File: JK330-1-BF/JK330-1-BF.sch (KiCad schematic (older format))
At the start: 16 parts, among them K1 CONN_2, K10 COLONETTE, K2 CONN_2, K3 CONN_3, K4 CONN_2, K5 COLONETTE, K6 COLONETTE, K7 COLONETTE, K8 COLONETTE, K9 COLONETTE, P1 U.FL, P2 U.FL, P3 U.FL, P4 CONN_5, P5 HE10-16, P6 CONN_6

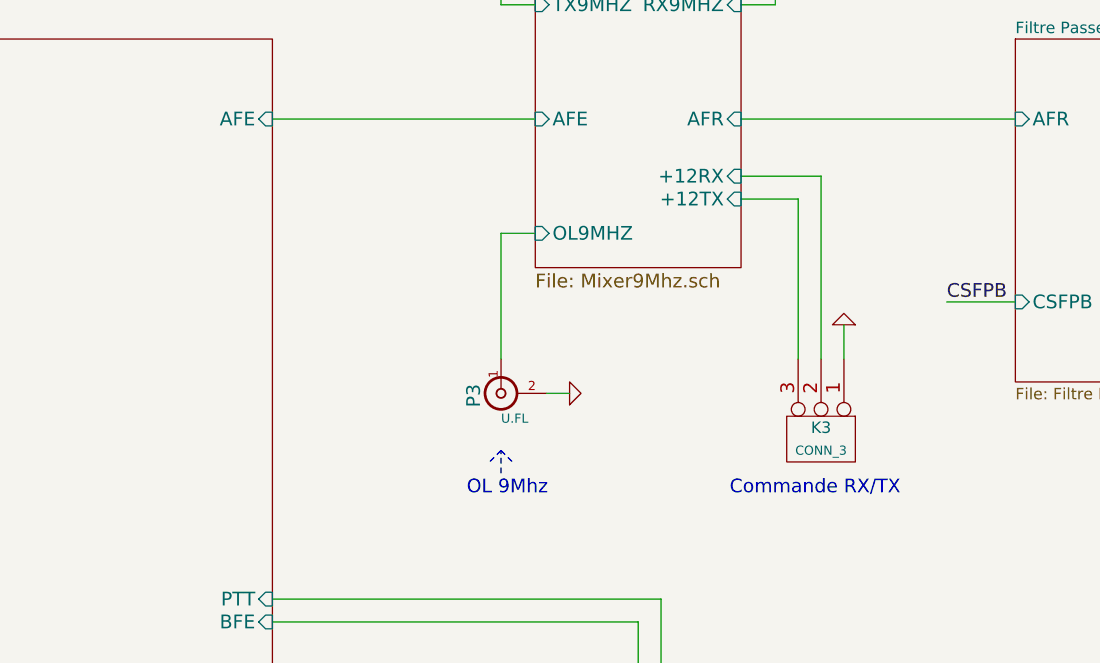
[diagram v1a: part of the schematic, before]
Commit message: Rajout commande PTT
+12VTV
+12VRX
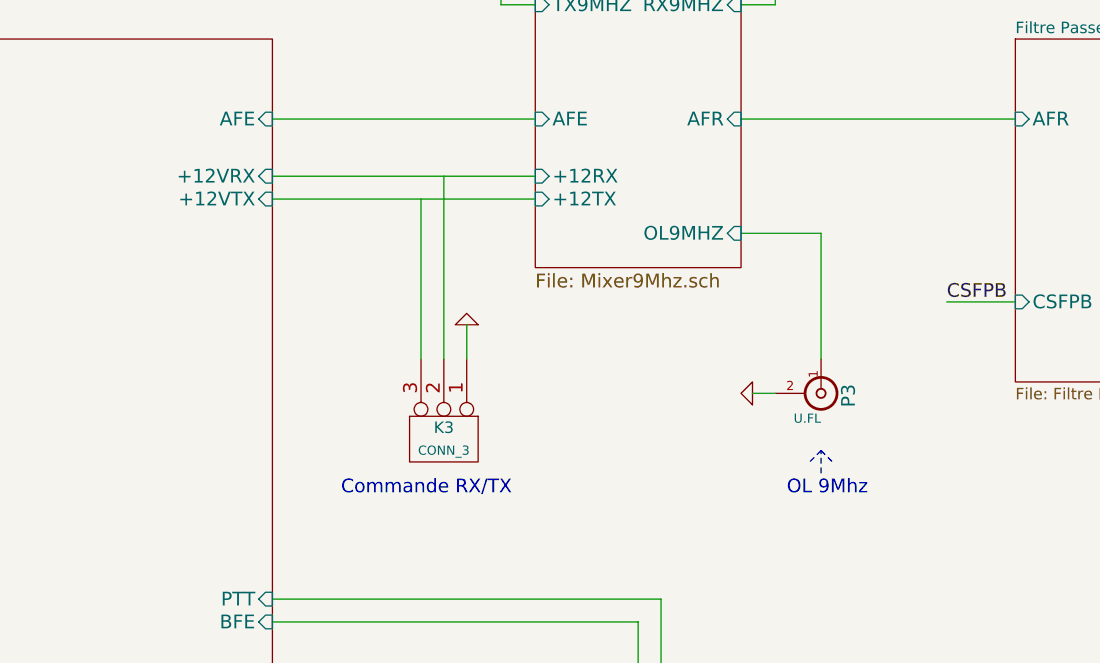
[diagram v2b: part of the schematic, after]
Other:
- moved on the sheet: K3, P3
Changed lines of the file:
@@
-EESchema Schematic File Version 2  date 29/04/2013 22:12:34
+EESchema Schematic File Version 2  date 30/04/2013 22:23:42
 LIBS:power
 LIBS:CEN-SCHEMA
@@
 Sheet 1 6
 Title ""
-Date "29 apr 2013"
+Date "30 apr 2013"
 Rev ""
 Comp ""
@@
 L GND #PWR01
 U 1 1 514E3278
-P 3950 3850
-F 0 "#PWR01" H 3950 3850 30  0001 C CNN
-F 1 "GND" H 3950 3780 30  0001 C CNN
-F 2 "" H 3950 3850 60  0001 C CNN
-F 3 "" H 3950 3850 60  0001 C CNN
-	1    3950 3850
-	0    -1   -1   0
+P 4750 3850
+F 0 "#PWR01" H 4750 3850 30  0001 C CNN
+F 1 "GND" H 4750 3780 30  0001 C CNN
+F 2 "" H 4750 3850 60  0001 C CNN
+F 3 "" H 4750 3850 60  0001 C CNN
+	1    4750 3850
+	0    1    -1   0
 $EndComp
 $Comp
@@
 $EndComp
 Wire Wire Line
-	3850 3850 3950 3850
-Wire Wire Line
-	4950 3700 4950 3000
-Wire Wire Line
-	4950 3000 4700 3000
-Wire Wire Line
-	3650 3700 3650 3150
-Wire Wire Line
-	3650 3150 3800 3150
+	4850 3850 4750 3850
+Wire Wire Line
+	3300 3700 3300 3000
+Wire Wire Line
+	5050 3700 5050 3150
 Wire Wire Line
 	3800 2650 2650 2650
@@
 	4700 2650 5900 2650
 Wire Wire Line
-	4700 2900 5050 2900
-Wire Wire Line
-	5050 2900 5050 3700
+	3400 2900 3400 3700
 Wire Wire Line
 	5850 6400 5850 6250
@@
 F0 "Mixer 9Mhz" 60
 F1 "Mixer9Mhz.sch" 60
-F2 "OL9MHZ" I L 3800 3150 60
-F3 "+12RX" I R 4700 2900 60
-F4 "+12TX" I R 4700 3000 60
+F2 "OL9MHZ" I R 4700 3150 60
+F3 "+12RX" I L 3800 2900 60
+F4 "+12TX" I L 3800 3000 60
 F5 "RX9MHZ" I R 4700 2150 60
 F6 "TX9MHZ" I L 3800 2150 60
@@
 F3 "BFE" I R 2650 4850 60
 F4 "AFE" I R 2650 2650 60
+F5 "+12VRX" I R 2650 2900 60
+F6 "+12VTX" I R 2650 3000 60
 $EndSheet
 Wire Notes Line
-	3650 4200 3650 4100
-Wire Notes Line
-	3650 4100 3600 4150
-Wire Notes Line
-	3650 4100 3700 4150
-Text Notes 3500 4300 0    60   ~ 0
+	5050 4200 5050 4100
+Wire Notes Line
+	5050 4100 5000 4150
+Wire Notes Line
+	5050 4100 5100 4150
+Text Notes 4900 4300 0    60   ~ 0
 OL 9Mhz
-Text Notes 4650 4300 0    60   ~ 0
+Text Notes 2950 4300 0    60   ~ 0
 Commande RX/TX\n
 $Comp
@@
 L CONN_3 K3
 U 1 1 514F8C00
-P 5050 4050
-F 0 "K3" V 5000 4050 50  0000 C CNN
-F 1 "CONN_3" V 5100 4050 40  0000 C CNN
-F 2 "" H 5050 4050 60  0000 C CNN
-F 3 "" H 5050 4050 60  0000 C CNN
-	1    5050 4050
-	0    1    1    0
-$EndComp
-Wire Wire Line
-	5150 3700 5150 3550
+P 3400 4050
+F 0 "K3" V 3350 4050 50  0000 C CNN
+F 1 "CONN_3" V 3450 4050 40  0000 C CNN
+F 2 "" H 3400 4050 60  0000 C CNN
+F 3 "" H 3400 4050 60  0000 C CNN
+	1    3400 4050
+	0    1    1    0
+$EndComp
+Wire Wire Line
+	3500 3700 3500 3550
 $Comp
 L GND #PWR014
 U 1 1 514F8DE0
-P 5150 3550
-F 0 "#PWR014" H 5150 3550 30  0001 C CNN
-F 1 "GND" H 5150 3480 30  0001 C CNN
-F 2 "" H 5150 3550 60  0000 C CNN
-F 3 "" H 5150 3550 60  0000 C CNN
-	1    5150 3550
+P 3500 3550
+F 0 "#PWR014" H 3500 3550 30  0001 C CNN
+F 1 "GND" H 3500 3480 30  0001 C CNN
+F 2 "" H 3500 3550 60  0000 C CNN
+F 3 "" H 3500 3550 60  0000 C CNN
+	1    3500 3550
 	-1   0    0    1
 $EndComp
@@
 L U.FL P3
 U 1 1 514F7AA8
-P 3650 3850
-F 0 "P3" H 3660 3970 60  0000 C CNN
-F 1 "U.FL" V 3760 3790 40  0000 C CNN
-F 2 "~" H 3650 3850 60  0000 C CNN
-F 3 "~" H 3650 3850 60  0000 C CNN
-	1    3650 3850
-	0    -1   1    0
+P 5050 3850
+F 0 "P3" H 5060 3970 60  0000 C CNN
+F 1 "U.FL" V 5160 3790 40  0000 C CNN
+F 2 "~" H 5050 3850 60  0000 C CNN
+F 3 "~" H 5050 3850 60  0000 C CNN
+	1    5050 3850
+	0    1    1    0
 $EndComp
 $Comp
@@
 	1    0    0    -1
 $EndComp
+Wire Wire Line
+	2650 2900 3800 2900
+Wire Wire Line
+	2650 3000 3800 3000
+Wire Wire Line
+	5050 3150 4700 3150
 $EndSCHEMATC

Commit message: Routage  PCB
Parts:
- added K11: CONN_3, symbol CONN_3
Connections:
- wire segments 54 -> 58
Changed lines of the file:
@@
-EESchema Schematic File Version 2  date 04/06/2013 21:43:31
+EESchema Schematic File Version 2  date 09/06/2013 23:13:58
 LIBS:power
 LIBS:CEN-SCHEMA
@@
 Sheet 1 6
 Title ""
-Date "4 jun 2013"
+Date "9 jun 2013"
 Rev ""
 Comp ""
@@
 F1 "Mixer9Mhz.sch" 60
 F2 "OL9MHZ" I R 4700 3150 60
-F3 "+12RX" I L 3800 2900 60
-F4 "+12TX" I L 3800 3000 60
-F5 "RX9MHZ" I R 4700 2150 60
-F6 "TX9MHZ" I L 3800 2150 60
-F7 "AFE" I L 3800 2650 60
-F8 "AFR" I R 4700 2650 60
+F3 "RX9MHZ" I R 4700 2150 60
+F4 "TX9MHZ" I L 3800 2150 60
+F5 "AFE" I L 3800 2650 60
+F6 "AFR" I R 4700 2650 60
+F7 "+12VRX" I L 3800 2900 60
+F8 "+12VTX" I L 3800 3000 60
 $EndSheet
 $Sheet
@@
 F1 "HP.sch" 50
 F2 "LINEOUT" I R 9650 2650 60
-F3 "AFRN" I L 8850 2650 60
-F4 "HP1" I R 9650 3300 60
-F5 "HP2" I R 9650 3550 60
+F3 "HP1" I R 9650 3300 60
+F4 "HP2" I R 9650 3550 60
+F5 "BFIN" I L 8850 2650 60
 $EndSheet
 Wire Wire Line
 	6750 2650 7450 2650
-Wire Wire Line
-	8300 2650 8850 2650
 Wire Wire Line
 	9650 3550 10100 3550
@@
 F 3 "" H 8150 6500 60  0000 C CNN
 	1    8150 6500
-	-1   0    0    1
+	1    0    0    1
 $EndComp
 Entry Wire Line
@@
 Wire Wire Line
 	5050 3150 4700 3150
+Connection ~ 3400 2900
+Connection ~ 3300 3000
+$Comp
+L CONN_3 K11
+U 1 1 51B4E722
+P 8600 1800
+F 0 "K11" V 8550 1800 50  0000 C CNN
+F 1 "CONN_3" V 8650 1800 40  0000 C CNN
+F 2 "" H 8600 1800 60  0000 C CNN
+F 3 "" H 8600 1800 60  0000 C CNN
+	1    8600 1800
+	0    -1   -1   0
+$EndComp
+Wire Wire Line
+	8300 2650 8600 2650
+Wire Wire Line
+	8600 2650 8600 2150
+Wire Wire Line
+	8850 2650 8700 2650
+Wire Wire Line
+	8700 2650 8700 2150
+Wire Wire Line
+	8500 2150 8500 2250
+$Comp
+L GND #PWR017
+U 1 1 51B4E972
+P 8500 2250
+F 0 "#PWR017" H 8500 2250 30  0001 C CNN
+F 1 "GND" H 8500 2180 30  0001 C CNN
+F 2 "" H 8500 2250 60  0000 C CNN
+F 3 "" H 8500 2250 60  0000 C CNN
+	1    8500 2250
+	1    0    0    -1
+$EndComp
 $EndSCHEMATC

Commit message: Reste 2 pistes a router
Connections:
- net labels removed: +BATT
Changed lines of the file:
@@
-EESchema Schematic File Version 2  date 09/06/2013 23:13:58
+EESchema Schematic File Version 2  date 11/06/2013 22:16:43
 LIBS:power
 LIBS:CEN-SCHEMA
@@
 Sheet 1 6
 Title ""
-Date "9 jun 2013"
+Date "11 jun 2013"
 Rev ""
 Comp ""
@@
 $EndComp
 $Comp
-L +BATT #PWR016
-U 1 1 514F93C1
-P 2500 6650
-F 0 "#PWR016" H 2500 6600 20  0001 C CNN
-F 1 "+BATT" H 2500 6750 30  0000 C CNN
-F 2 "" H 2500 6650 60  0000 C CNN
-F 3 "" H 2500 6650 60  0000 C CNN
-	1    2500 6650
-	1    0    0    -1
-$EndComp
-$Comp
 L U.FL P1
 U 1 1 514F77BA
@@
 F 3 "" H 8600 1800 60  0000 C CNN
 	1    8600 1800
-	0    -1   -1   0
-$EndComp
-Wire Wire Line
-	8300 2650 8600 2650
-Wire Wire Line
-	8600 2650 8600 2150
-Wire Wire Line
-	8850 2650 8700 2650
-Wire Wire Line
-	8700 2650 8700 2150
-Wire Wire Line
-	8500 2150 8500 2250
-$Comp
-L GND #PWR017
+	0    1    -1   0
+$EndComp
+Wire Wire Line
+	8700 2150 8700 2250
+$Comp
+L GND #PWR016
 U 1 1 51B4E972
-P 8500 2250
-F 0 "#PWR017" H 8500 2250 30  0001 C CNN
-F 1 "GND" H 8500 2180 30  0001 C CNN
-F 2 "" H 8500 2250 60  0000 C CNN
-F 3 "" H 8500 2250 60  0000 C CNN
-	1    8500 2250
-	1    0    0    -1
-$EndComp
+P 8700 2250
+F 0 "#PWR016" H 8700 2250 30  0001 C CNN
+F 1 "GND" H 8700 2180 30  0001 C CNN
+F 2 "" H 8700 2250 60  0000 C CNN
+F 3 "" H 8700 2250 60  0000 C CNN
+	1    8700 2250
+	1    0    0    -1
+$EndComp
+Wire Wire Line
+	8300 2650 8500 2650
+Wire Wire Line
+	8500 2650 8500 2150
+Wire Wire Line
+	8600 2150 8600 2650
+Wire Wire Line
+	8600 2650 8850 2650
+$Comp
+L +12V #PWR017
+U 1 1 51B7A15D
+P 2500 6650
+F 0 "#PWR017" H 2500 6600 20  0001 C CNN
+F 1 "+12V" H 2500 6750 30  0000 C CNN
+F 2 "" H 2500 6650 60  0000 C CNN
+F 3 "" H 2500 6650 60  0000 C CNN
+	1    2500 6650
+	1    0    0    -1
+$EndComp

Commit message: Fin Routage PCb V0-10
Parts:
- removed K4: CONN_2, symbol CONN_2
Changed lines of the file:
@@
-EESchema Schematic File Version 2  date 16/06/2013 19:24:33
+EESchema Schematic File Version 2
 LIBS:power
 LIBS:CEN-SCHEMA
@@
 encoding utf-8
 Sheet 1 6
-Title ""
-Date "16 jun 2013"
-Rev ""
-Comp ""
-Comment1 ""
+Title "JK330 "
+Date "18 jun 2013"
+Rev "V0.10"
+Comp "F4DEB 2013"
+Comment1 "CARTE FI 9Mhz FILTRE BF"
 Comment2 ""
 Comment3 ""
@@
 $EndComp
 $Comp
-L CONN_2 K4
-U 1 1 514F92A0
-P 2250 6750
-F 0 "K4" H 2550 6900 50  0000 C CNN
-F 1 "CONN_2" H 2600 6850 40  0000 C CNN
-F 2 "" H 2250 6750 60  0000 C CNN
-F 3 "" H 2250 6750 60  0000 C CNN
-	1    2250 6750
-	-1   0    0    1
-$EndComp
-Wire Wire Line
-	2250 6650 2500 6650
-Wire Wire Line
-	2250 6750 2500 6750
-$Comp
-L GND #PWR2
-U 1 1 514F93B2
-P 2500 6750
-F 0 "#PWR2" H 2500 6750 30  0001 C CNN
-F 1 "GND" H 2500 6680 30  0001 C CNN
-F 2 "" H 2500 6750 60  0000 C CNN
-F 3 "" H 2500 6750 60  0000 C CNN
-	1    2500 6750
-	0    -1   -1   0
-$EndComp
-$Comp
 L U.FL P1
 U 1 1 514F77BA
@@
 Wire Wire Line
 	8600 2650 8850 2650
-$Comp
-L +12V #PWR1
-U 1 1 51B7A15D
-P 2500 6650
-F 0 "#PWR1" H 2500 6600 20  0001 C CNN
-F 1 "+12V" H 2500 6750 30  0000 C CNN
-F 2 "" H 2500 6650 60  0000 C CNN
-F 3 "" H 2500 6650 60  0000 C CNN
-	1    2500 6650
-	1    0    0    -1
-$EndComp
 $EndSCHEMATC
